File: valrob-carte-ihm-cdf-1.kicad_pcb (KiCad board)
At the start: 2 copper layers, 55 x 75 mm, 85 parts, among them J1 USB_C_Receptacle_USB2.0_14P, J2 Conn_01x02, J3 Conn_01x02, J4 Conn_01x04_Pin, J5 Conn_01x04_Pin, J6 Conn_01x04_Pin, SW1 SW_Push, SW2 SW_Push, SW3 SW_DIP_x04, SW4 SW_SPDT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

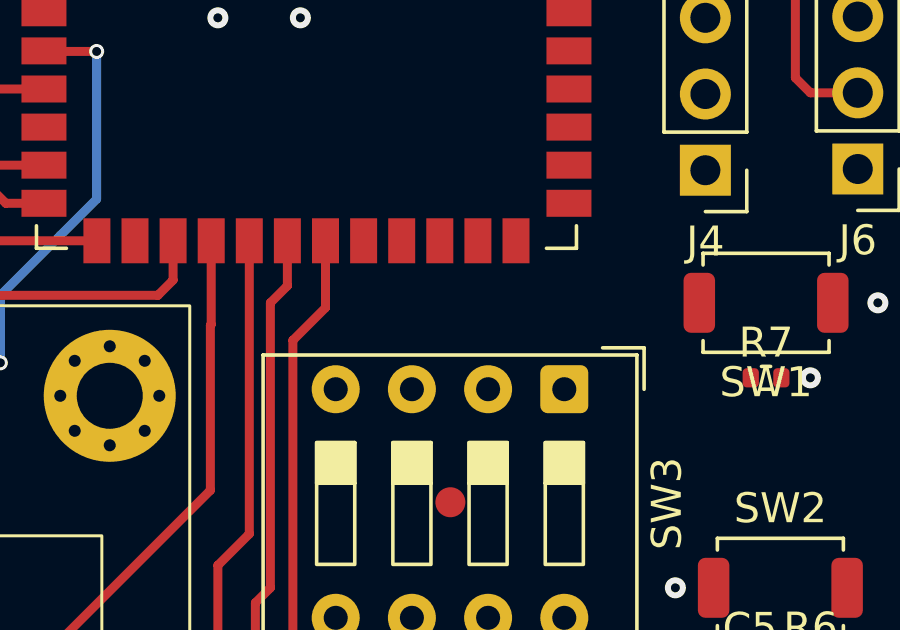
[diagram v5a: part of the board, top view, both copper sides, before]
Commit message: pcb: add DIP switches routing
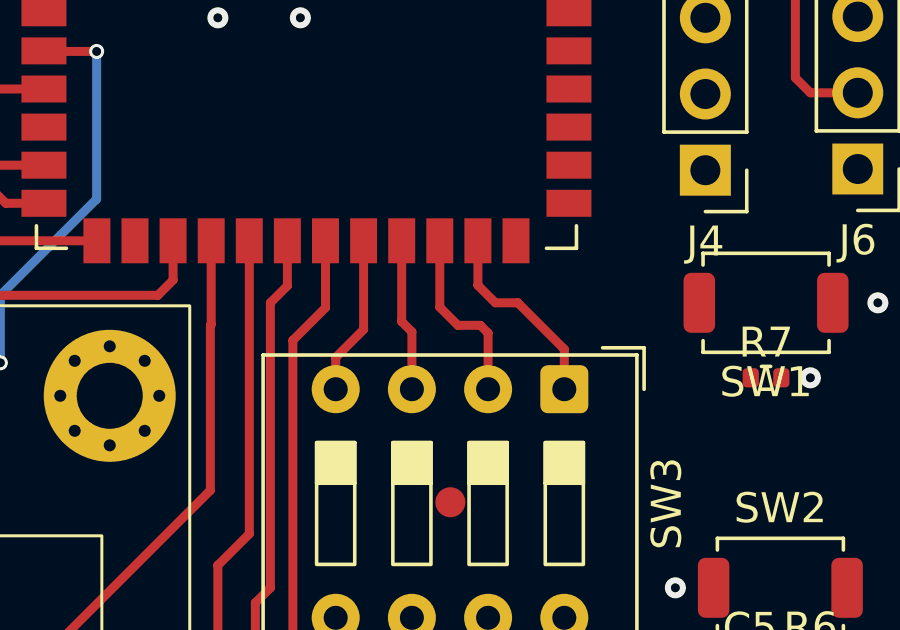
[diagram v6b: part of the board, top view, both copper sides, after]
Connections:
- SW3 pad 1: Net-(U4-GPIO45) -> Net-(U4-GPIO48/SPICLK_N/SUBSPICLK_N_DIFF)
- SW3 pad 2: Net-(U4-GPIO48/SPICLK_N/SUBSPICLK_N_DIFF) -> Net-(U4-GPIO47/SPICLK_P/SUBSPICLK_P_DIFF)
- SW3 pad 3: Net-(U4-GPIO47/SPICLK_P/SUBSPICLK_P_DIFF) -> Net-(U4-GPIO21)
- SW3 pad 4: Net-(U4-GPIO21) -> Net-(U4-GPIO14/TOUCH14/ADC2_CH3/FSPIWP/FSPIDQS/SUBSPIWP)
- U4 pad 22: /RGB_LEDS -> Net-(U4-GPIO14/TOUCH14/ADC2_CH3/FSPIWP/FSPIDQS/SUBSPIWP)
- U4 pad 26: Net-(U4-GPIO45) -> /RGB_LEDS
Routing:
- net Net-(U4-GPIO48/SPICLK_N/SUBSPICLK_N_DIFF): track 0.00 -> 6.58 mm
- net Net-(U4-GPIO47/SPICLK_P/SUBSPICLK_P_DIFF): track 0.00 -> 6.05 mm
- net Net-(U4-GPIO14/TOUCH14/ADC2_CH3/FSPIWP/FSPIDQS/SUBSPIWP): track 0.00 -> 5.33 mm
- net Net-(U4-GPIO21): track 0.00 -> 5.09 mm

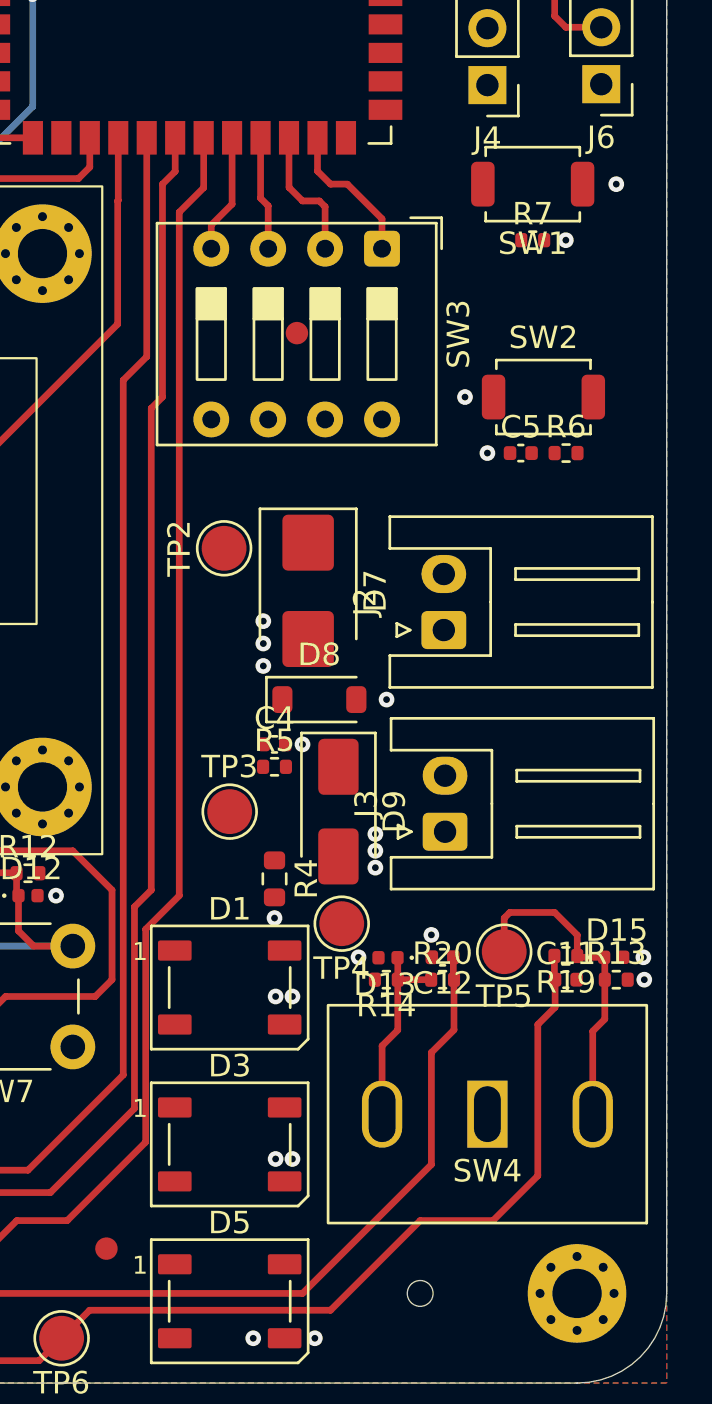
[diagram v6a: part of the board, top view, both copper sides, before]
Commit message: pcb: add RGB leds routing
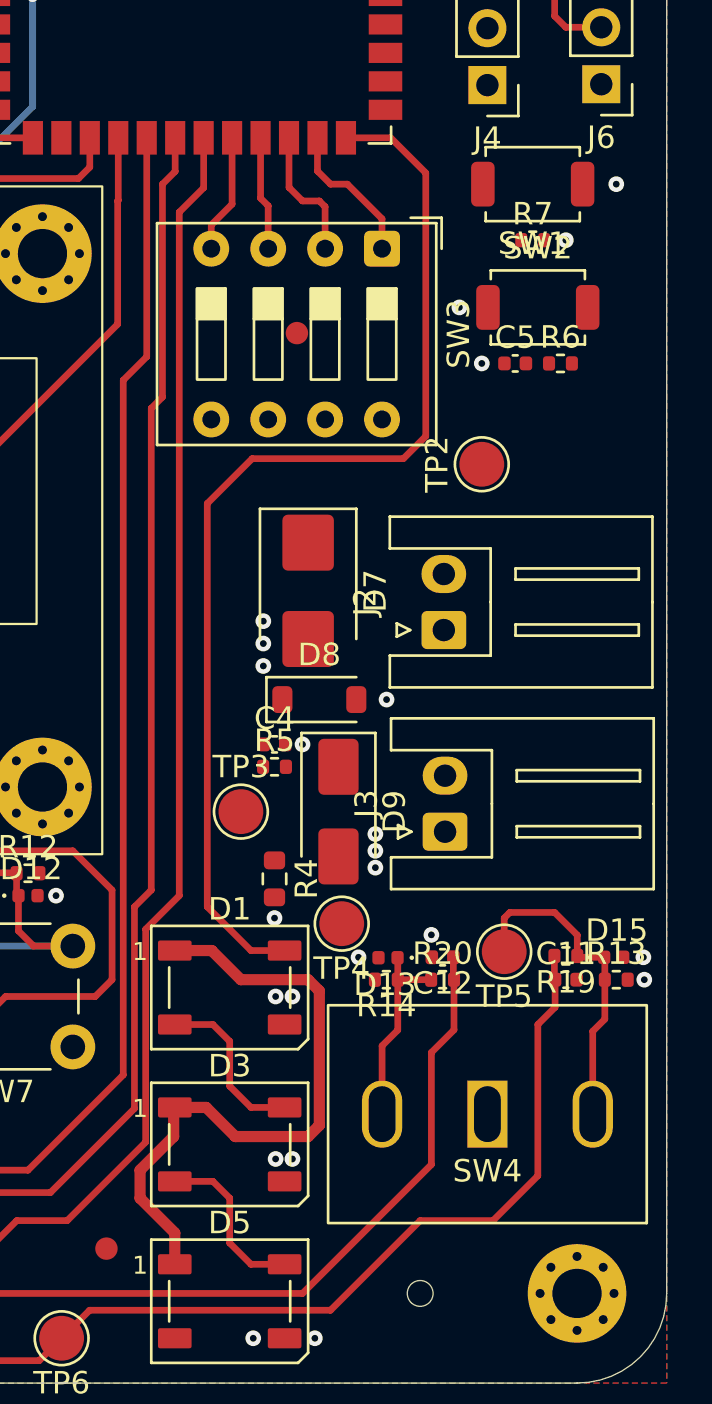
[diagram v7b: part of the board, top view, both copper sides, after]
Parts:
- moved TP2 12.1 mm to (165.8, 102.0)
- moved C5 4.01 mm to (167.2, 97.5)
- moved R6 4.01 mm to (169.3, 97.5)
- moved SW2 4.01 mm to (168.2, 95.0)
- moved TP3 0.50 mm to (155.0, 117.5)
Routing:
- net /RGB_LEDS: track 0.00 -> 49.2 mm
- net +5V: track 4.58 -> 33.3 mm
- net Net-(D1-DOUT): track 0.00 -> 7.60 mm
- net Net-(D3-DOUT): track 0.00 -> 7.60 mm

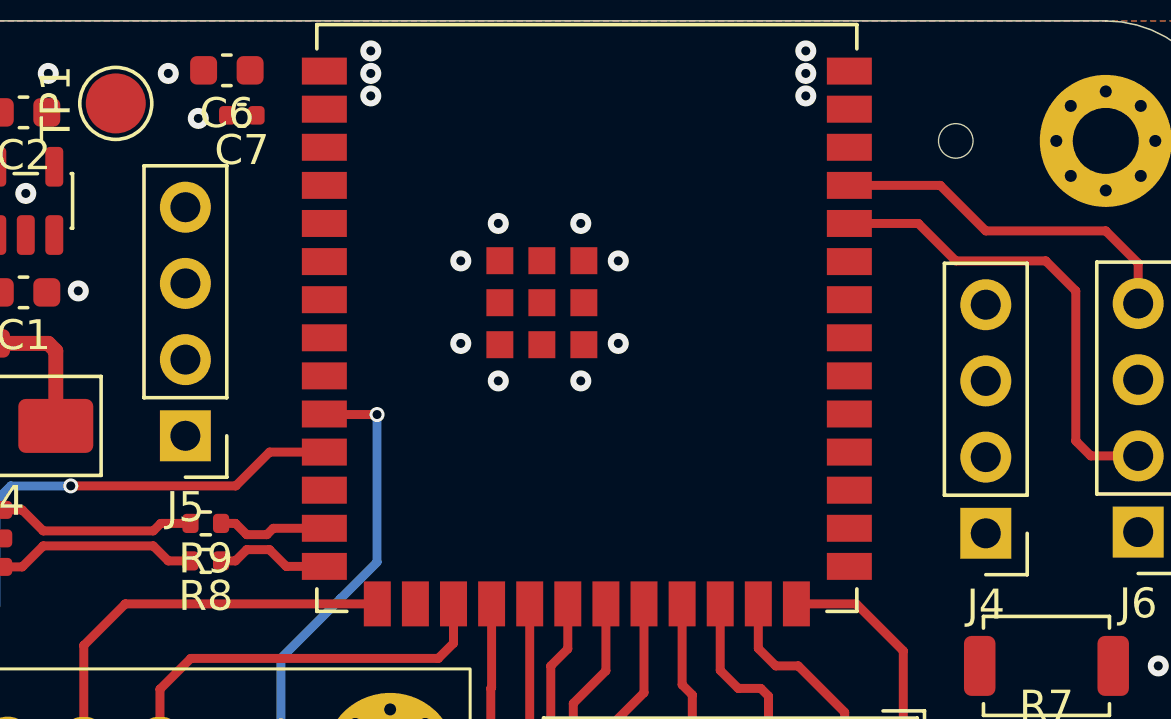
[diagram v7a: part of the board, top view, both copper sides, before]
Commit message: pcb: add spare GPIO routing
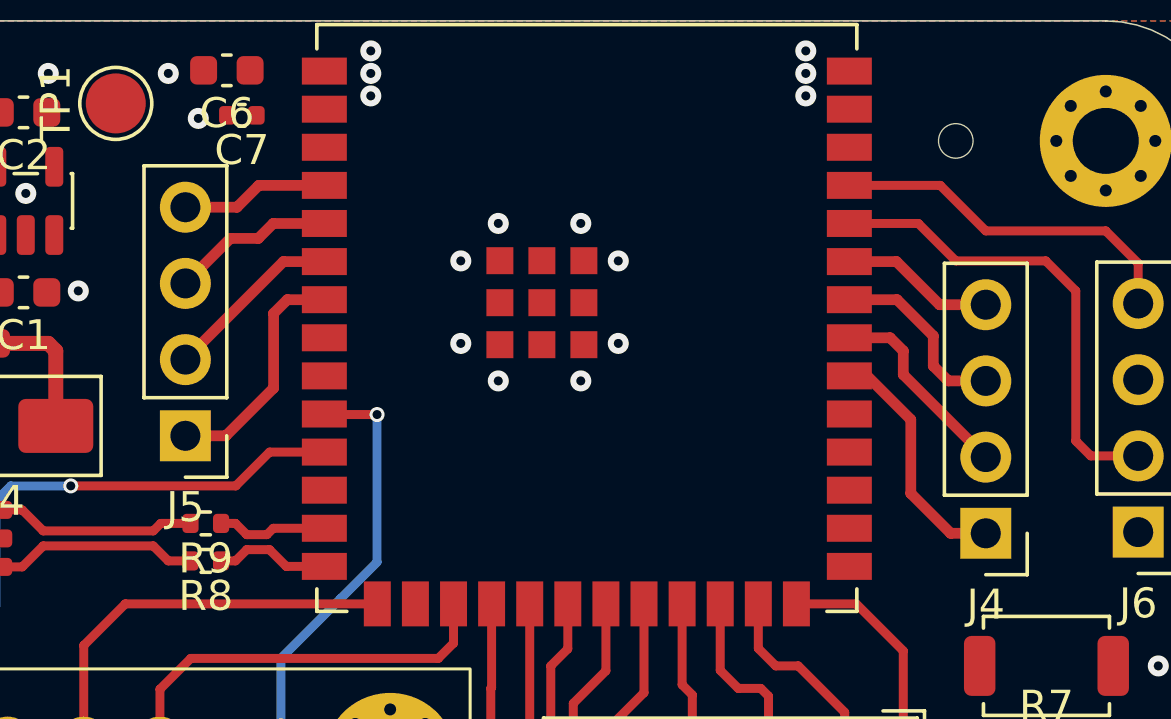
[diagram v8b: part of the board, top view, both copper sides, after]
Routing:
- net Net-(J4-Pin_1): track 0.00 -> 8.16 mm
- net Net-(J5-Pin_1): track 0.00 -> 7.97 mm
- net Net-(J4-Pin_2): track 0.00 -> 6.66 mm
- net Net-(J4-Pin_3): track 0.00 -> 6.25 mm
- net Net-(J5-Pin_2): track 0.00 -> 5.99 mm
- net Net-(J5-Pin_3): track 0.00 -> 5.46 mm
- net Net-(J4-Pin_4): track 0.00 -> 5.14 mm
- net Net-(J5-Pin_4): track 0.00 -> 4.93 mm
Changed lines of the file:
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@@
+	)
+	(segment
+		(start 163.25 79.79)
+		(end 163.25 79)
+		(width 0.359)
+		(layer "F.Cu")
+		(net 29)
+	)
+	(segment
+		(start 163.25 79)
+		(end 162.8125 78.5625)
+		(width 0.359)
+		(layer "F.Cu")
+		(net 29)
+	)
+	(segment
+		(start 162.8125 78.5625)
+		(end 161.4525 78.5625)
+		(width 0.359)
+		(layer "F.Cu")
+		(net 29)
+	)
+	(segment
+		(start 166 82.54)
+		(end 163.25 79.79)
+		(width 0.359)
+		(layer "F.Cu")
+		(net 29)
+	)
+	(segment
+		(start 164.25 78.5)
+		(end 163.0425 77.2925)
+		(width 0.359)
+		(layer "F.Cu")
+		(net 30)
+	)
+	(segment
+		(start 164.75 80)
+		(end 164.25 79.5)
+		(width 0.359)
+		(layer "F.Cu")
+		(net 30)
+	)
+	(segment
+		(start 164.25 79.5)
+		(end 164.25 78.5)
+		(width 0.359)
+		(layer "F.Cu")
+		(net 30)
+	)
+	(segment
+		(start 166 80)
+		(end 164.75 80)
+		(width 0.359)
+		(layer "F.Cu")
+		(net 30)
+	)
+	(segment
+		(start 163.0425 77.2925)
+		(end 161.4525 77.2925)
+		(width 0.359)
+		(layer "F.Cu")
+		(net 30)
+	)
+	(segment
+		(start 164.83 85.08)
+		(end 163.5 83.75)
+		(width 0.359)
+		(layer "F.Cu")
+		(net 31)
+	)
+	(segment
+		(start 162.0435 79.8325)
+		(end 161.4525 79.8325)
+		(width 0.359)
+		(layer "F.Cu")
+		(net 31)
+	)
+	(segment
+		(start 163.5 83.75)
+		(end 163.5 81.289)
+		(width 0.359)
+		(layer "F.Cu")
+		(net 31)
+	)
+	(segment
+		(start 163.5 81.289)
+		(end 162.0435 79.8325)
+		(width 0.359)
+		(layer "F.Cu")
+		(net 31)
+	)
+	(segment
+		(start 166 85.08)
+		(end 164.83 85.08)
+		(width 0.359)
+		(layer "F.Cu")
+		(net 31)
+	)
+	(segment
+		(start 164.46 77.46)
+		(end 163.0225 76.0225)
+		(width 0.359)
+		(layer "F.Cu")
+		(net 32)
+	)
+	(segment
+		(start 163.0225 76.0225)
+		(end 161.4525 76.0225)
+		(width 0.359)
+		(layer "F.Cu")
+		(net 32)
+	)
+	(segment
+		(start 166 77.46)
+		(end 164.46 77.46)
+		(width 0.359)
+		(layer "F.Cu")
+		(net 32)
+	)
+	(segment
+		(start 139.32 76.75)
+		(end 140.82 75.25)
+		(width 0.359)
+		(layer "F.Cu")
+		(net 33)
+	)
+	(segment
+		(start 141.75 75.25)
+		(end 142.2475 74.7525)
+		(width 0.359)
+		(layer "F.Cu")
+		(net 33)
+	)
+	(segment
+		(start 142.2475 74.7525)
+		(end 143.9525 74.7525)
+		(width 0.359)
+		(layer "F.Cu")
+		(net 33)
+	)
+	(segment
+		(start 140.82 75.25)
+		(end 141.75 75.25)
+		(width 0.359)
+		(layer "F.Cu")
+		(net 33)
+	)
+	(segment
+		(start 142.5875 76.0225)
+		(end 143.9525 76.0225)
+		(width 0.359)
+		(layer "F.Cu")
+		(net 34)
+	)
+	(segment
+		(start 139.32 79.29)
+		(end 142.5875 76.0225)
+		(width 0.359)
+		(layer "F.Cu")
+		(net 34)
+	)
+	(segment
+		(start 141.04 74.21)
+		(end 141.7675 73.4825)
+		(width 0.359)
+		(layer "F.Cu")
+		(net 35)
+	)
+	(segment
+		(start 139.32 74.21)
+		(end 141.04 74.21)
+		(width 0.359)
+		(layer "F.Cu")
+		(net 35)
+	)
+	(segment
+		(start 141.7675 73.4825)
+		(end 143.9525 73.4825)
+		(width 0.359)
+		(layer "F.Cu")
+		(net 35)
+	)
+	(segment
+		(start 142.26 77.75)
+		(end 142.7175 77.2925)
+		(width 0.359)
+		(layer "F.Cu")
+		(net 36)
+	)
+	(segment
+		(start 142.7175 77.2925)
+		(end 143.9525 77.2925)
+		(width 0.359)
+		(layer "F.Cu")
+		(net 36)
+	)
+	(segment
+		(start 139.32 81.83)
+		(end 140.67 81.83)
+		(width 0.359)
+		(layer "F.Cu")
+		(net 36)
+	)
+	(segment
+		(start 142.26 80.24)
+		(end 142.26 77.75)
+		(width 0.359)
+		(layer "F.Cu")
+		(net 36)
+	)
+	(segment
+		(start 140.67 81.83)
+		(end 142.26 80.24)
+		(width 0.359)
+		(layer "F.Cu")
+		(net 36)
 	)
 	(segment
